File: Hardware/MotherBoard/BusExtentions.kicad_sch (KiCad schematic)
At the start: 10 parts, among them J3 ISA00, J4 ISA10, J7 ISA01, J8 ISA11, U10 74HCT541, U11 SN74LVC245AN, U12 SN74LVC245AN, U13 74HCT541, U14 74HCT541, U9 74HCT541

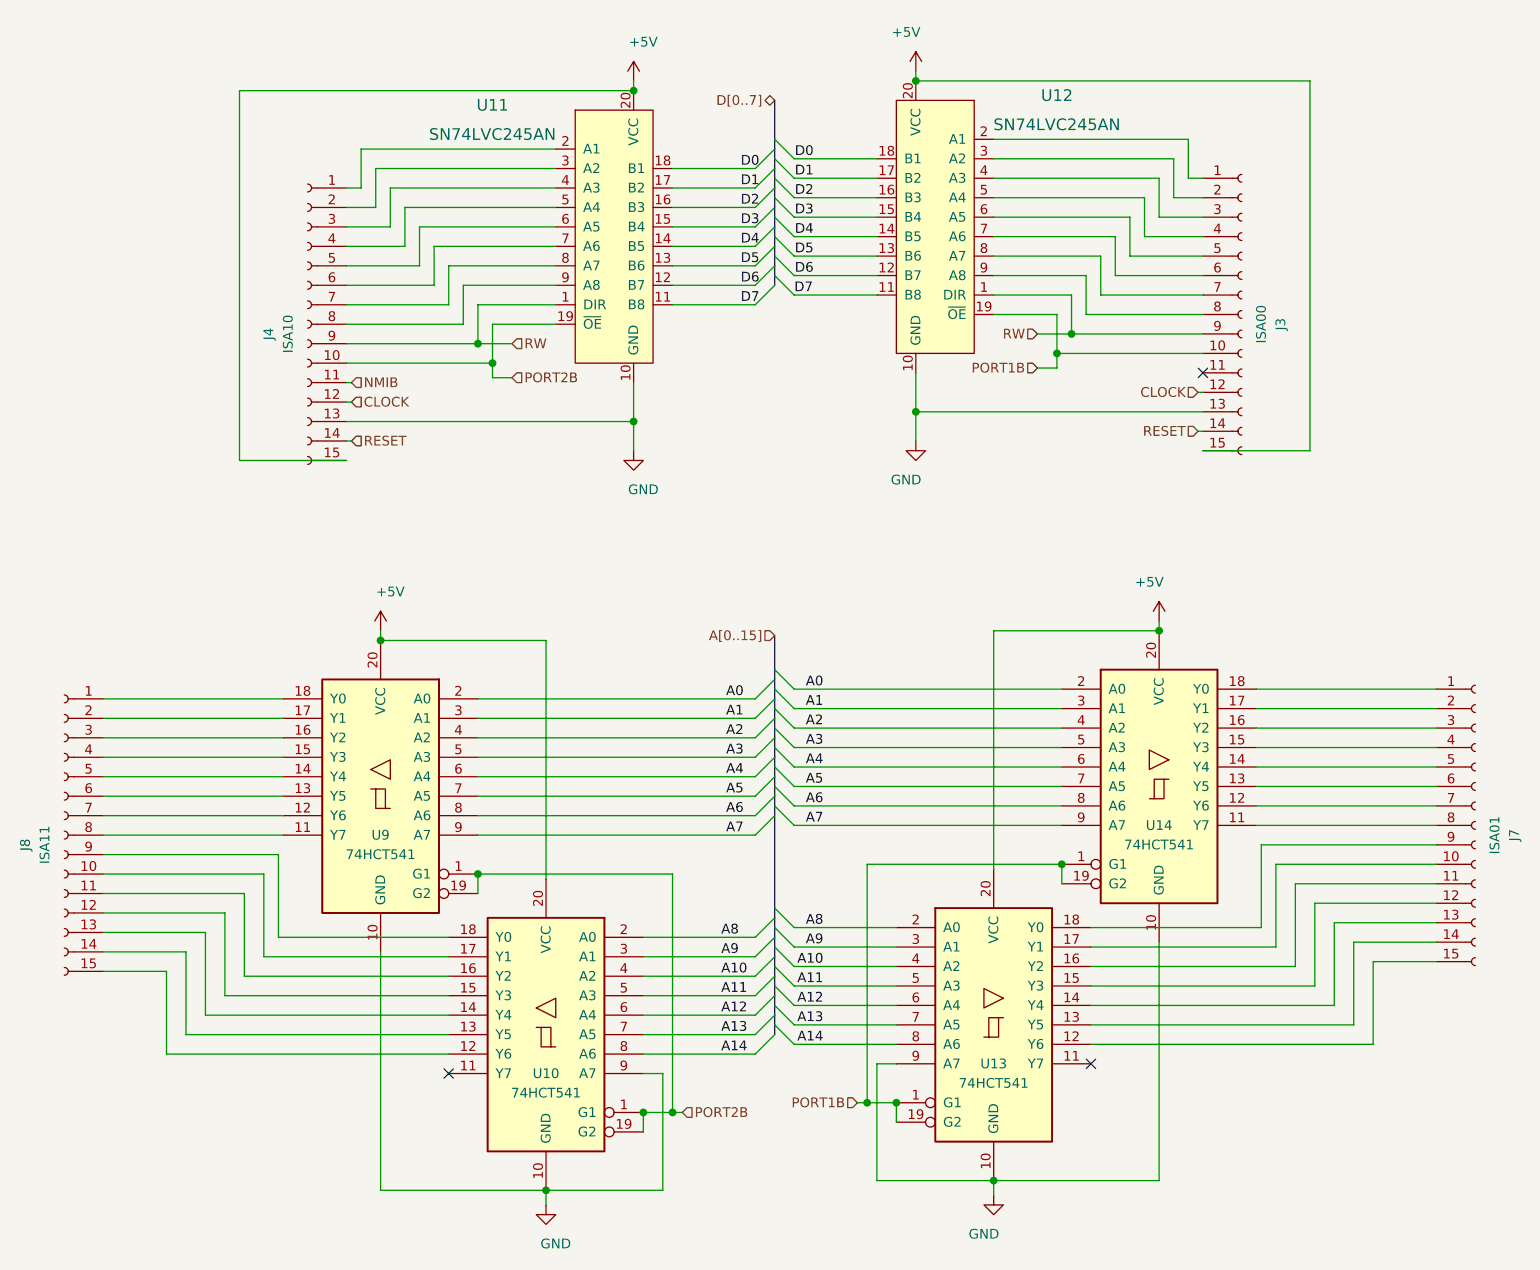
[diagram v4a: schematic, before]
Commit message: Implement APU and fix schematics
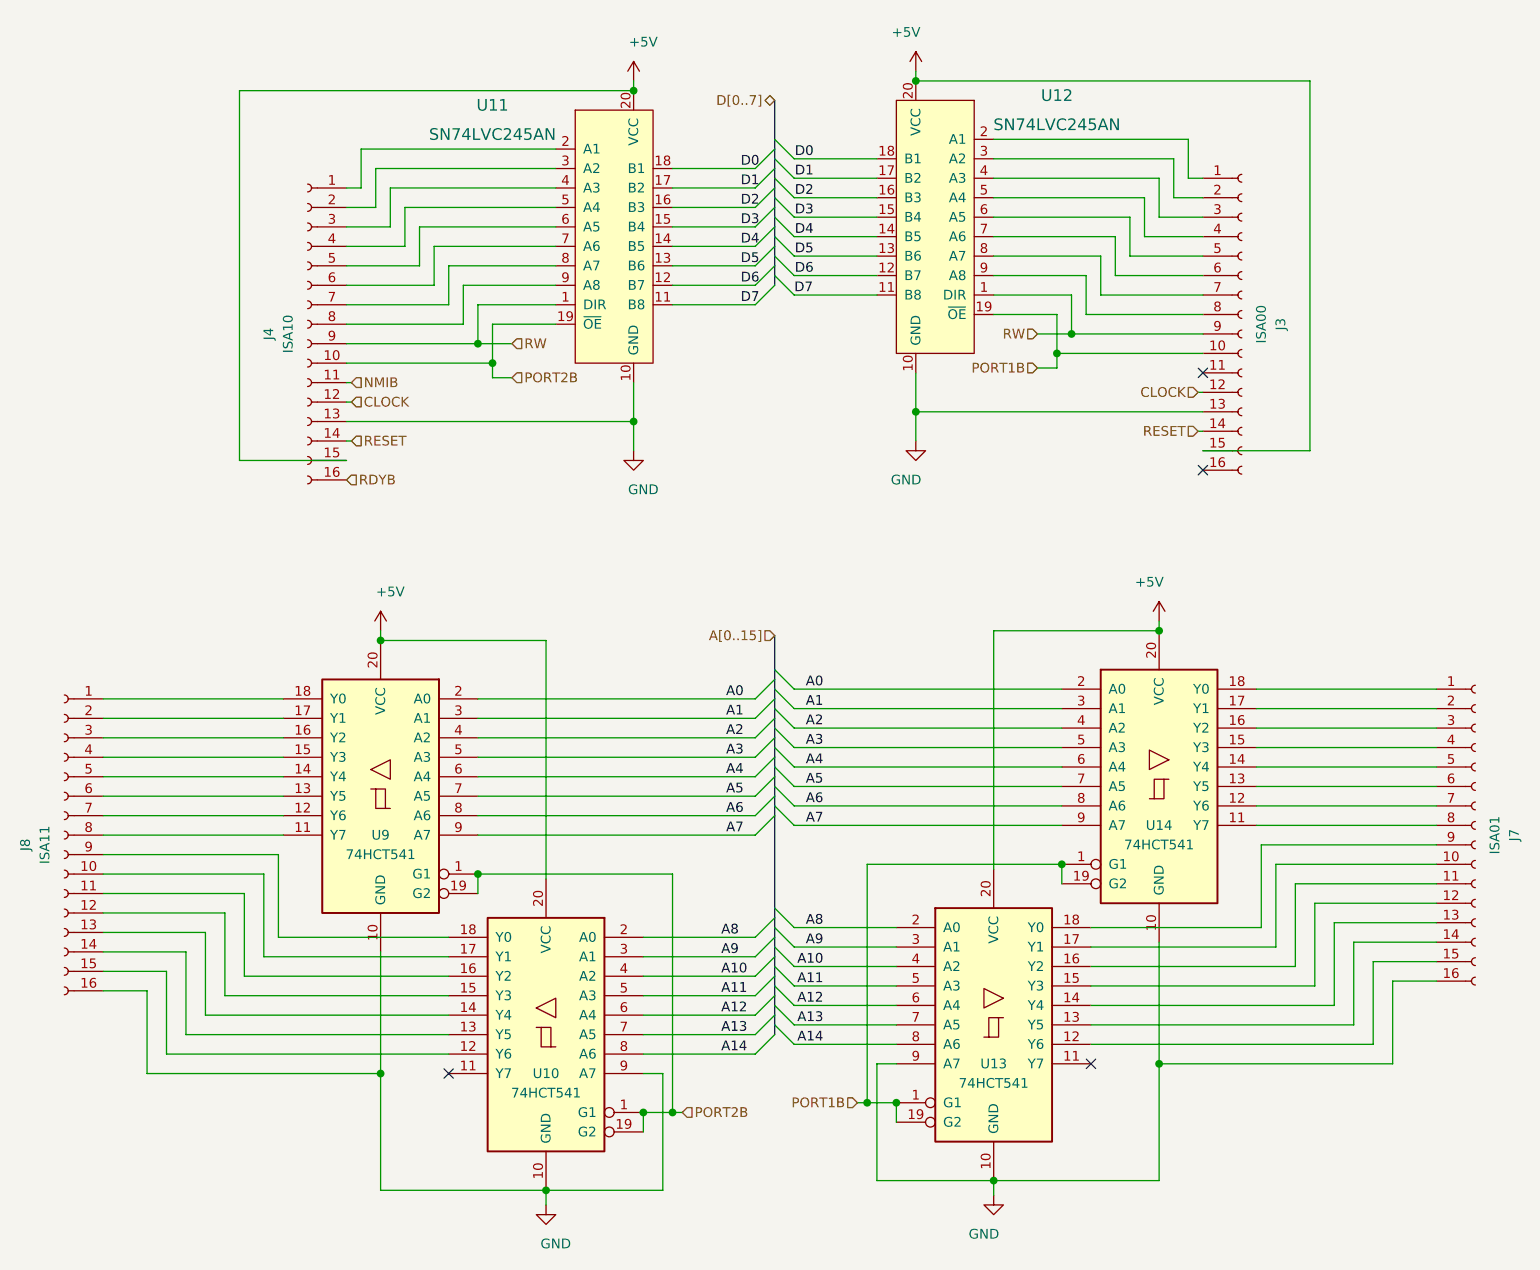
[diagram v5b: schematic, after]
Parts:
- J3, J4, J7, J8: footprint Connector_PinSocket_2.54mm:PinSocket_1x15_P2.54mm_Vertical -> Connector_PinSocket_2.54mm:PinSocket_1x16_P2.54mm_Vertical; symbol Connector:Conn_01x15_Female -> Connector:Conn_01x16_Female
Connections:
- net GND: now also J7.16 (Pin_16), J8.16 (Pin_16)
- new net RDYB: J4.16 (Pin_16)
- no-connect marks 3 -> 4
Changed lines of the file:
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@@
   (paper "A4")
   (junction (at 63.5 100.33) (diameter 1.016) (color 0 0 0 0))
+  (junction (at 63.5 156.845) (diameter 1.016) (color 0 0 0 0))
   (junction (at 76.2 61.595) (diameter 1.016) (color 0 0 0 0))
   (junction (at 76.2 130.81) (diameter 1.016) (color 0 0 0 0))
@@
   (junction (at 153.67 60.325) (diameter 1.016) (color 0 0 0 0))
   (junction (at 165.1 99.06) (diameter 1.016) (color 0 0 0 0))
+  (junction (at 165.1 155.575) (diameter 1.016) (color 0 0 0 0))
+  (no_connect (at 170.815 78.105))
   (no_connect (at 156.21 155.575))
   (no_connect (at 170.815 65.405))
@@
     (stroke (width 0) (type solid) (color 0 0 0 0))
   )
+  (wire (pts (xy 27.305 146.05) (xy 33.02 146.05))
+    (stroke (width 0) (type solid) (color 0 0 0 0))
+  )
+  (wire (pts (xy 33.02 146.05) (xy 33.02 156.845))
+    (stroke (width 0) (type solid) (color 0 0 0 0))
+  )
+  (wire (pts (xy 33.02 156.845) (xy 63.5 156.845))
+    (stroke (width 0) (type solid) (color 0 0 0 0))
+  )
   (wire (pts (xy 35.56 154.305) (xy 35.56 143.51))
     (stroke (width 0) (type solid) (color 0 0 0 0))
@@
     (stroke (width 0) (type solid) (color 0 0 0 0))
   )
-  (wire (pts (xy 63.5 140.97) (xy 63.5 172.085))
+  (wire (pts (xy 63.5 140.97) (xy 63.5 156.845))
+    (stroke (width 0) (type solid) (color 0 0 0 0))
+  )
+  (wire (pts (xy 63.5 156.845) (xy 63.5 172.085))
     (stroke (width 0) (type solid) (color 0 0 0 0))
   )
@@
     (stroke (width 0) (type solid) (color 0 0 0 0))
   )
-  (wire (pts (xy 165.1 139.7) (xy 165.1 170.815))
+  (wire (pts (xy 165.1 139.7) (xy 165.1 155.575))
+    (stroke (width 0) (type solid) (color 0 0 0 0))
+  )
+  (wire (pts (xy 165.1 155.575) (xy 165.1 170.815))
     (stroke (width 0) (type solid) (color 0 0 0 0))
   )
@@
     (stroke (width 0) (type solid) (color 0 0 0 0))
   )
+  (wire (pts (xy 195.58 144.78) (xy 195.58 155.575))
+    (stroke (width 0) (type solid) (color 0 0 0 0))
+  )
+  (wire (pts (xy 195.58 155.575) (xy 165.1 155.575))
+    (stroke (width 0) (type solid) (color 0 0 0 0))
+  )
+  (wire (pts (xy 201.295 144.78) (xy 195.58 144.78))
+    (stroke (width 0) (type solid) (color 0 0 0 0))
+  )
   (bus (pts (xy 114.935 29.845) (xy 114.935 34.925))
     (stroke (width 0) (type solid) (color 0 0 0 0))
@@
   (label "A14" (at 121.285 153.035 180)
     (effects (font (size 1.27 1.27)) (justify right bottom))
+  )
+  (hierarchical_label "RDYB" (shape input) (at 59.055 79.375 0)
+    (effects (font (size 1.27 1.27)) (justify left))
   )
   (hierarchical_label "NMIB" (shape input) (at 59.69 66.675 0)
@@
     )
   )
-  (symbol (lib_id "Connector:Conn_01x15_Female") (at 22.225 125.73 0) (mirror y) (unit 1)
+  (symbol (lib_id "Connector:Conn_01x16_Female") (at 22.225 125.73 0) (mirror y) (unit 1)
     (in_bom yes) (on_board yes)
     (property "Reference" "J8" (id 0) (at 17.145 127 90))
     (property "Value" "ISA11" (id 1) (at 19.685 127 90))
-    (property "Footprint" "Connector_PinSocket_2.54mm:PinSocket_1x15_P2.54mm_Vertical" (id 2) (at 22.225 125.73 0)
-      (effects (font (size 1.27 1.27)) hide)
-    )
-    (property "Datasheet" "~" (id 3) (at 22.225 125.73 0)
-      (effects (font (size 1.27 1.27)) hide)
-    )
-  )
-  (symbol (lib_name "Connector:Conn_01x15_Female_2") (lib_id "Connector:Conn_01x15_Female") (at 53.975 59.055 0) (mirror y) (unit 1)
+    (property "Footprint" "Connector_PinSocket_2.54mm:PinSocket_1x16_P2.54mm_Vertical" (id 2) (at 22.225 125.73 0)
+      (effects (font (size 1.27 1.27)) hide)
+    )
+    (property "Datasheet" "" (id 3) (at 22.225 125.73 0)
+      (effects (font (size 1.27 1.27)) hide)
+    )
+  )
+  (symbol (lib_name "Connector:Conn_01x15_Female_2") (lib_id "Connector:Conn_01x16_Female") (at 53.975 59.055 0) (mirror y) (unit 1)
     (in_bom yes) (on_board yes)
     (property "Reference" "J4" (id 0) (at 48.895 60.325 90))
     (property "Value" "ISA10" (id 1) (at 51.435 60.325 90))
-    (property "Footprint" "Connector_PinSocket_2.54mm:PinSocket_1x15_P2.54mm_Vertical" (id 2) (at 53.975 59.055 0)
-      (effects (font (size 1.27 1.27)) hide)
-    )
-    (property "Datasheet" "~" (id 3) (at 53.975 59.055 0)
-      (effects (font (size 1.27 1.27)) hide)
-    )
-  )
-  (symbol (lib_name "Connector:Conn_01x15_Female_1") (lib_id "Connector:Conn_01x15_Female") (at 175.895 57.785 0) (unit 1)
+    (property "Footprint" "Connector_PinSocket_2.54mm:PinSocket_1x16_P2.54mm_Vertical" (id 2) (at 53.975 59.055 0)
+      (effects (font (size 1.27 1.27)) hide)
+    )
+    (property "Datasheet" "" (id 3) (at 53.975 59.055 0)
+      (effects (font (size 1.27 1.27)) hide)
+    )
+  )
+  (symbol (lib_name "Connector:Conn_01x15_Female_1") (lib_id "Connector:Conn_01x16_Female") (at 175.895 57.785 0) (unit 1)
     (in_bom yes) (on_board yes)
     (property "Reference" "J3" (id 0) (at 180.975 59.055 90))
     (property "Value" "ISA00" (id 1) (at 178.435 59.055 90))
-    (property "Footprint" "Connector_PinSocket_2.54mm:PinSocket_1x15_P2.54mm_Vertical" (id 2) (at 175.895 57.785 0)
-      (effects (font (size 1.27 1.27)) hide)
-    )
-    (property "Datasheet" "~" (id 3) (at 175.895 57.785 0)
-      (effects (font (size 1.27 1.27)) hide)
-    )
-  )
-  (symbol (lib_name "Connector:Conn_01x15_Female_3") (lib_id "Connector:Conn_01x15_Female") (at 206.375 124.46 0) (unit 1)
+    (property "Footprint" "Connector_PinSocket_2.54mm:PinSocket_1x16_P2.54mm_Vertical" (id 2) (at 175.895 57.785 0)
+      (effects (font (size 1.27 1.27)) hide)
+    )
+    (property "Datasheet" "" (id 3) (at 175.895 57.785 0)
+      (effects (font (size 1.27 1.27)) hide)
+    )
+  )
+  (symbol (lib_name "Connector:Conn_01x15_Female_3") (lib_id "Connector:Conn_01x16_Female") (at 206.375 124.46 0) (unit 1)
     (in_bom yes) (on_board yes)
     (property "Reference" "J7" (id 0) (at 211.455 125.73 90))
     (property "Value" "ISA01" (id 1) (at 208.915 125.73 90))
-    (property "Footprint" "Connector_PinSocket_2.54mm:PinSocket_1x15_P2.54mm_Vertical" (id 2) (at 206.375 124.46 0)
-      (effects (font (size 1.27 1.27)) hide)
-    )
-    (property "Datasheet" "~" (id 3) (at 206.375 124.46 0)
-      (effects (font (size 1.27 1.27)) hide)
-    )
+    (property "Footprint" "Connector_PinSocket_2.54mm:PinSocket_1x16_P2.54mm_Vertical" (id 2) (at 206.375 124.46 0)
+      (effects (font (size 1.27 1.27)) hide)
+    )
+    (property "Datasheet" "" (id 3) (at 206.375 124.46 0)
+      (effects (font (size 1.27 1.27)) hide)
+    )

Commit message: Implement DMA and PCB ports
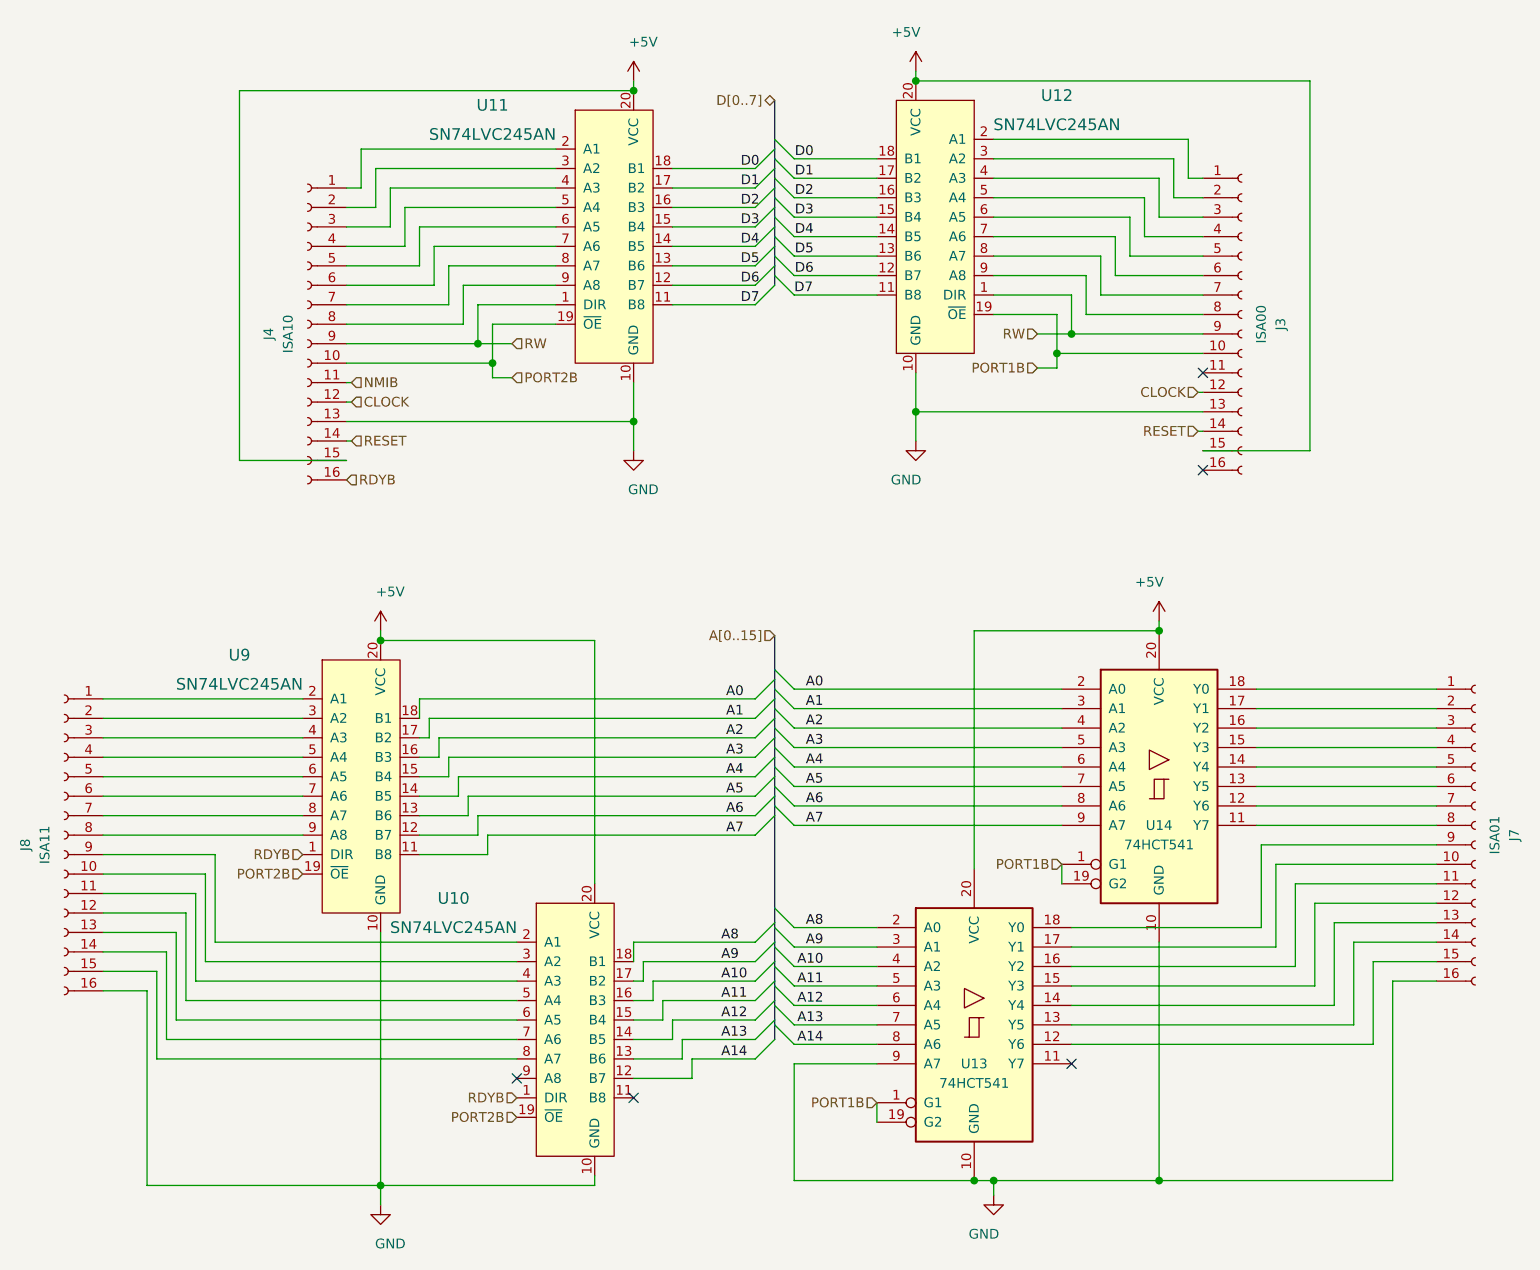
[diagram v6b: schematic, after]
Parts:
- removed U10, U9: 74HCT541, Package_DIP:DIP-20_W7.62mm, symbol 74xx:74HCT541
- added U10, U9: SN74LVC245AN, Package_DIP:DIP-20_W7.62mm, symbol dk_Logic-Buffers-Drivers-Receivers-Transceivers:SN74LVC245AN
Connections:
- net +5V: now also U10.20 (VCC), U9.20 (VCC)
- net A0: now also U9.18 (B1)
- net A1: now also U9.17 (B2)
- net A10: now also U10.16 (B3)
- net A11: now also U10.15 (B4)
- net A12: now also U10.14 (B5)
- net A13: now also U10.13 (B6)
- net A14: now also U10.12 (B7)
- net A2: now also U9.16 (B3)
- net A3: now also U9.15 (B4)
- net A4: now also U9.14 (B5)
- net A5: now also U9.13 (B6)
- net A6: now also U9.12 (B7)
- net A7: now also U9.11 (B8)
- net A8: now also U10.18 (B1)
- net A9: now also U10.17 (B2)
- net GND: now also U10.10 (GND), U9.10 (GND)
- net PORT2B: now also U10.19 (~OE), U9.19 (~OE)
- net RDYB: now also U10.1 (DIR), U9.1 (DIR)
- net at J8.1 (Pin_1): now also U9.2 (A1)
- net at J8.10 (Pin_10): now also U10.3 (A2)
- net at J8.11 (Pin_11): now also U10.4 (A3)
- net at J8.12 (Pin_12): now also U10.5 (A4)
- net at J8.13 (Pin_13): now also U10.6 (A5)
- net at J8.14 (Pin_14): now also U10.7 (A6)
- net at J8.15 (Pin_15): now also U10.8 (A7)
- net at J8.2 (Pin_2): now also U9.3 (A2)
- net at J8.3 (Pin_3): now also U9.4 (A3)
- net at J8.4 (Pin_4): now also U9.5 (A4)
- net at J8.5 (Pin_5): now also U9.6 (A5)
- net at J8.6 (Pin_6): now also U9.7 (A6)
- net at J8.7 (Pin_7): now also U9.8 (A7)
- net at J8.8 (Pin_8): now also U9.9 (A8)
- net at J8.9 (Pin_9): now also U10.2 (A1)
- no-connect marks 4 -> 5
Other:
- moved on the sheet: U13
